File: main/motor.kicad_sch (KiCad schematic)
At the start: 8 parts, among them J3 motor_L, J4 motor_R, U4 DRV8835

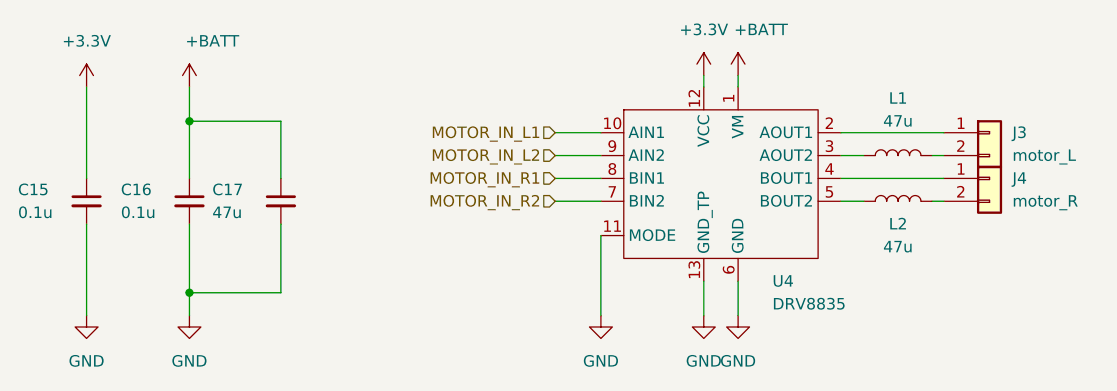
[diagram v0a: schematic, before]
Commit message: feat: update main board
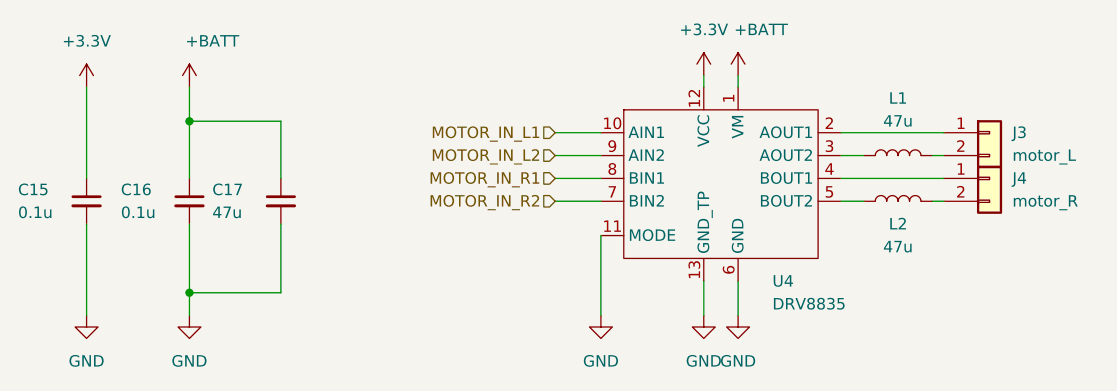
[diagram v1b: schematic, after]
